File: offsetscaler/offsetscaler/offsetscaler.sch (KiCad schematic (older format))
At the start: 34 parts, among them J1 IN 1, J2 OUT 1, J3 INV OUT 1, J4 EURO_PWR_2x5, J5 IN 2, J6 OUT 2, J7 INV OUT 2, U1 TL074

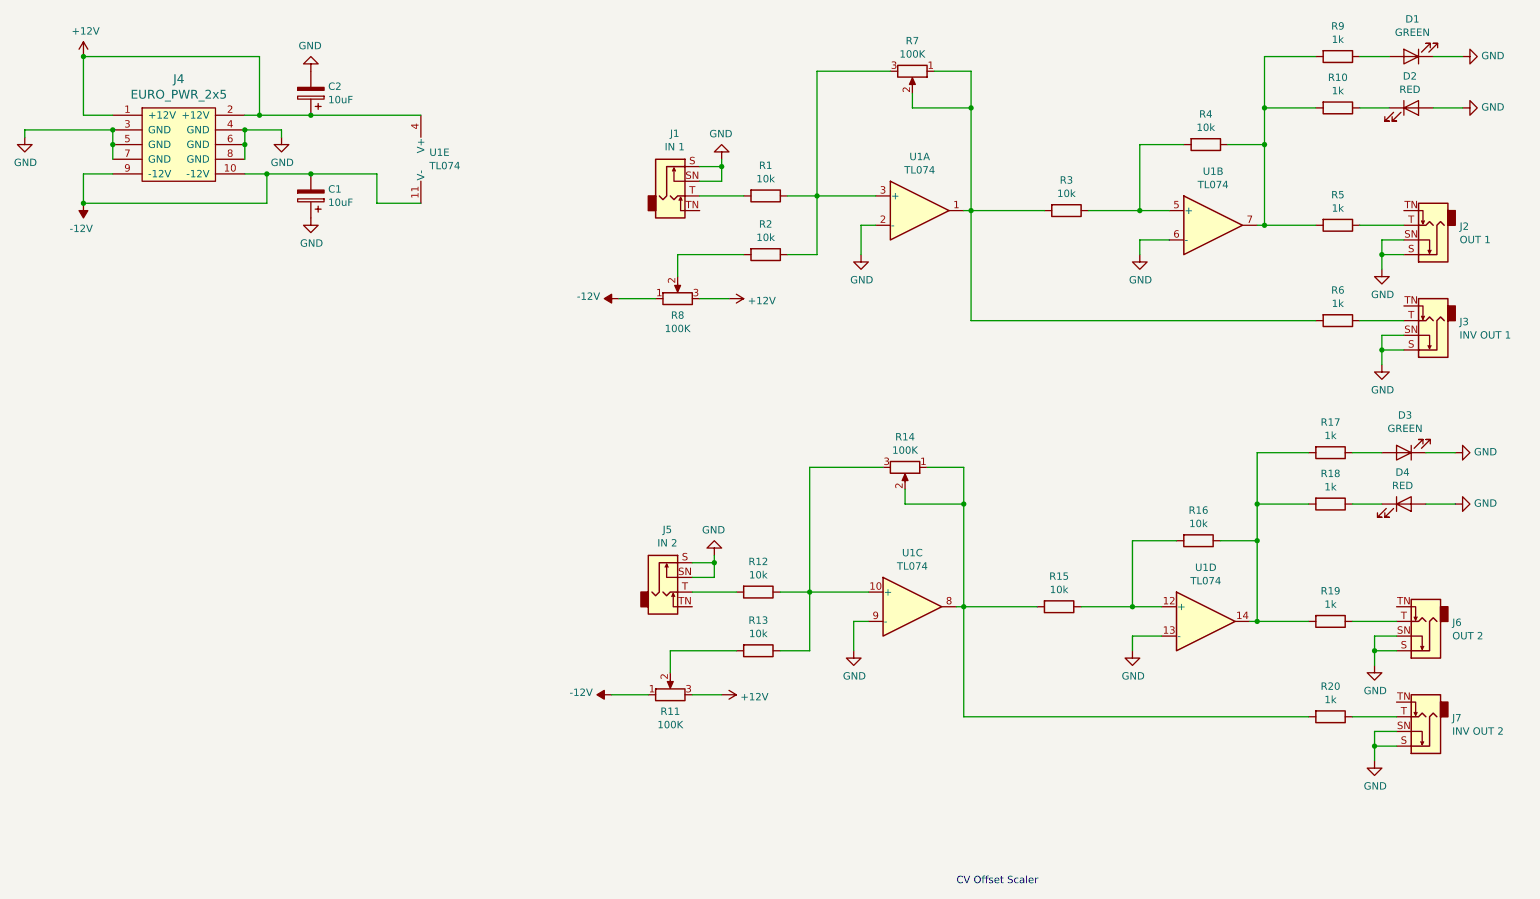
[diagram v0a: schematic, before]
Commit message: Fixed offsetscaler and added some megasequencer ideas and resources
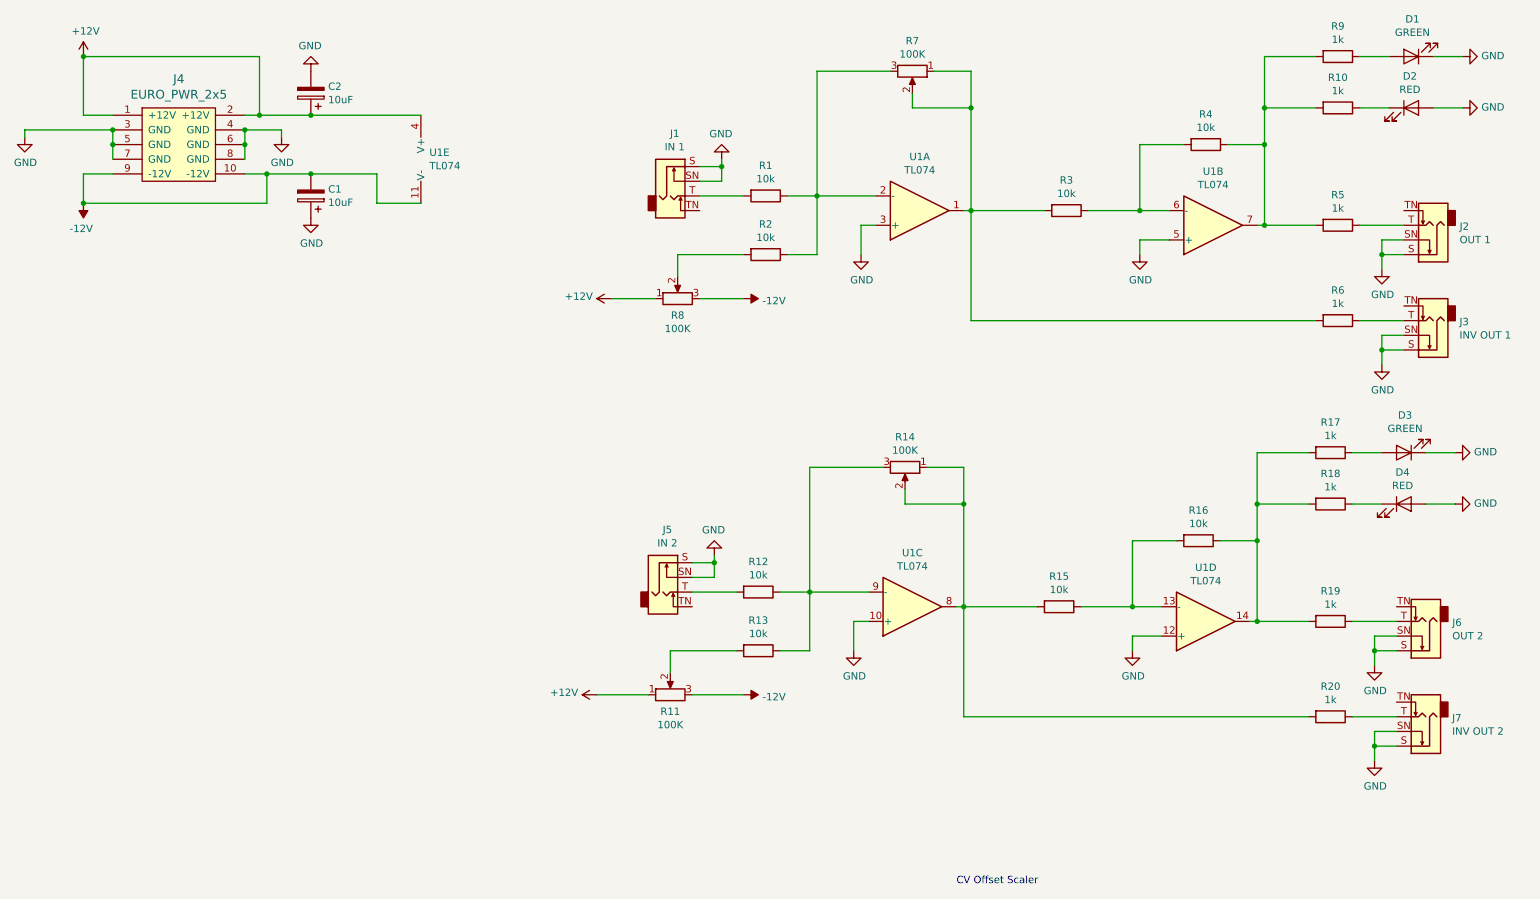
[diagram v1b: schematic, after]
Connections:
- net +12V: now also R11.1, R8.1; no longer R11.3, R8.3
- net -12V: now also R11.3, R8.3; no longer R11.1, R8.1
- net GND: now also U1.10 (+), U1.12 (+), U1.3 (+), U1.5 (+); no longer U1.13 (-), U1.2 (-), U1.6 (-), U1.9 (-)
- net at R1.1, R2.1, R7.3: now also U1.2 (-); no longer U1.3 (+)
- net at R3.1, R4.2: now also U1.6 (-); no longer U1.5 (+)
- net at R12.1, R13.1, R14.3: now also U1.9 (-); no longer U1.10 (+)
- net at R15.1, R16.2: now also U1.13 (-); no longer U1.12 (+)
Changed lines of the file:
@@
-$Comp
-L Amplifier_Operational:TL074 U1
-U 1 1 5D91D523
-P 6800 2100
-F 0 "U1" H 6800 2467 50  0000 C CNN
-F 1 "TL074" H 6800 2376 50  0000 C CNN
-F 2 "Package_DIP:DIP-14_W7.62mm_LongPads" H 6800 2100 50  0001 C CNN
-F 3 "http://www.ti.com/lit/ds/symlink/tl071.pdf" H 6800 2100 50  0001 C CNN
-	1    6800 2100
-	1    0    0    -1
-$EndComp
 $Comp
 L Amplifier_Operational:TL074 U1
 U 2 1 5D91D69A
 P 8800 2200
-F 0 "U1" H 8800 2567 50  0000 C CNN
-F 1 "TL074" H 8800 2476 50  0000 C CNN
+F 0 "U1" H 8800 1833 50  0000 C CNN
+F 1 "TL074" H 8800 1924 50  0000 C CNN
 F 2 "Package_DIP:DIP-14_W7.62mm_LongPads" H 8800 2200 50  0001 C CNN
 F 3 "http://www.ti.com/lit/ds/symlink/tl071.pdf" H 8800 2200 50  0001 C CNN
 	2    8800 2200
-	1    0    0    -1
+	1    0    0    1
 $EndComp
 $Comp
@@
 	1    0    0    -1
 $EndComp
-Wire Wire Line
-	8500 2300 8300 2300
-Wire Wire Line
-	8300 2300 8300 2400
-Wire Wire Line
-	6500 2200 6400 2200
-Wire Wire Line
-	6400 2200 6400 2400
 $Comp
 L Connector:AudioJack2_Switch J1
@@
 L power:+12V #PWR0108
 U 1 1 5D922076
-P 5500 2700
-F 0 "#PWR0108" H 5500 2550 50  0001 C CNN
-F 1 "+12V" V 5515 2828 50  0000 L CNN
-F 2 "" H 5500 2700 50  0001 C CNN
-F 3 "" H 5500 2700 50  0001 C CNN
-	1    5500 2700
-	0    1    1    0
+P 4700 2700
+F 0 "#PWR0108" H 4700 2550 50  0001 C CNN
+F 1 "+12V" V 4715 2828 50  0000 L CNN
+F 2 "" H 4700 2700 50  0001 C CNN
+F 3 "" H 4700 2700 50  0001 C CNN
+	1    4700 2700
+	0    -1   -1   0
 $EndComp
 $Comp
 L power:-12V #PWR0109
 U 1 1 5D9220B9
-P 4750 2700
-F 0 "#PWR0109" H 4750 2800 50  0001 C CNN
-F 1 "-12V" V 4765 2828 50  0000 L CNN
-F 2 "" H 4750 2700 50  0001 C CNN
-F 3 "" H 4750 2700 50  0001 C CNN
-	1    4750 2700
-	0    -1   -1   0
-$EndComp
-Wire Wire Line
-	4750 2700 5000 2700
-Wire Wire Line
-	5300 2700 5500 2700
+P 5600 2700
+F 0 "#PWR0109" H 5600 2800 50  0001 C CNN
+F 1 "-12V" V 5615 2828 50  0000 L CNN
+F 2 "" H 5600 2700 50  0001 C CNN
+F 3 "" H 5600 2700 50  0001 C CNN
+	1    5600 2700
+	0    1    1    0
+$EndComp
 $Comp
 L Device:R R2
@@
 	6100 2400 6100 2000
 Connection ~ 6100 2000
-Wire Wire Line
-	6100 2000 6500 2000
 $Comp
 L Device:R_POT R7
@@
 Wire Wire Line
 	8300 1650 8300 2100
-Connection ~ 8300 2100
-Wire Wire Line
-	8300 2100 8500 2100
 Wire Wire Line
 	8900 1650 9150 1650
@@
 	1    0    0    -1
 $EndComp
-Wire Wire Line
-	7100 2100 7150 2100
-Connection ~ 9150 2200
-Wire Wire Line
-	9150 2200 9100 2200
 Wire Wire Line
 	9150 2200 9500 2200
@@
 U 3 1 5D97E513
 P 6750 4800
-F 0 "U1" H 6750 5167 50  0000 C CNN
-F 1 "TL074" H 6750 5076 50  0000 C CNN
+F 0 "U1" H 6750 4433 50  0000 C CNN
+F 1 "TL074" H 6750 4524 50  0000 C CNN
 F 2 "Package_DIP:DIP-14_W7.62mm_LongPads" H 6750 4800 50  0001 C CNN
 F 3 "http://www.ti.com/lit/ds/symlink/tl071.pdf" H 6750 4800 50  0001 C CNN
 	3    6750 4800
-	1    0    0    -1
+	1    0    0    1
 $EndComp
 $Comp
@@
 U 4 1 5D97E519
 P 8750 4900
-F 0 "U1" H 8750 5267 50  0000 C CNN
-F 1 "TL074" H 8750 5176 50  0000 C CNN
+F 0 "U1" H 8750 4533 50  0000 C CNN
+F 1 "TL074" H 8750 4624 50  0000 C CNN
 F 2 "Package_DIP:DIP-14_W7.62mm_LongPads" H 8750 4900 50  0001 C CNN
 F 3 "http://www.ti.com/lit/ds/symlink/tl071.pdf" H 8750 4900 50  0001 C CNN
 	4    8750 4900
-	1    0    0    -1
+	1    0    0    1
 $EndComp
 $Comp
@@
 Wire Wire Line
 	8250 5000 8250 5100
-Wire Wire Line
-	6450 4900 6350 4900
-Wire Wire Line
-	6350 4900 6350 5100
 $Comp
 L Connector:AudioJack2_Switch J5
@@
 L power:+12V #PWR0117
 U 1 1 5D97E54E
-P 5450 5400
-F 0 "#PWR0117" H 5450 5250 50  0001 C CNN
-F 1 "+12V" V 5465 5528 50  0000 L CNN
-F 2 "" H 5450 5400 50  0001 C CNN
-F 3 "" H 5450 5400 50  0001 C CNN
-	1    5450 5400
-	0    1    1    0
+P 4600 5400
+F 0 "#PWR0117" H 4600 5250 50  0001 C CNN
+F 1 "+12V" V 4615 5528 50  0000 L CNN
+F 2 "" H 4600 5400 50  0001 C CNN
+F 3 "" H 4600 5400 50  0001 C CNN
+	1    4600 5400
+	0    -1   -1   0
 $EndComp
 $Comp
 L power:-12V #PWR0118
 U 1 1 5D97E554
-P 4700 5400
-F 0 "#PWR0118" H 4700 5500 50  0001 C CNN
-F 1 "-12V" V 4715 5528 50  0000 L CNN
-F 2 "" H 4700 5400 50  0001 C CNN
-F 3 "" H 4700 5400 50  0001 C CNN
-	1    4700 5400
-	0    -1   -1   0
-$EndComp
-Wire Wire Line
-	4700 5400 4950 5400
-Wire Wire Line
-	5250 5400 5450 5400
+P 5600 5400
+F 0 "#PWR0118" H 5600 5500 50  0001 C CNN
+F 1 "-12V" V 5615 5528 50  0000 L CNN
+F 2 "" H 5600 5400 50  0001 C CNN
+F 3 "" H 5600 5400 50  0001 C CNN
+	1    5600 5400
+	0    1    1    0
+$EndComp
 $Comp
 L Device:R R13
@@
 	6050 5100 6050 4700
 Connection ~ 6050 4700
-Wire Wire Line
-	6050 4700 6450 4700
 $Comp
 L Device:R_POT R14
@@
 	1    0    0    -1
 $EndComp
-Wire Wire Line
-	7050 4800 7100 4800
 Connection ~ 9100 4900
 Wire Wire Line
@@
 	2650 1450 3400 1450
 $Comp
-L power:GND #PWR?
+L power:GND #PWR0123
 U 1 1 5D9C92D6
 P 2650 1150
-F 0 "#PWR?" H 2650 900 50  0001 C CNN
+F 0 "#PWR0123" H 2650 900 50  0001 C CNN
 F 1 "GND" H 2655 977 50  0000 C CNN
 F 2 "" H 2650 1150 50  0001 C CNN
@@
 $EndComp
 $Comp
-L power:GND #PWR?
+L power:GND #PWR0124
 U 1 1 5D9C9379
 P 2650 2150
-F 0 "#PWR?" H 2650 1900 50  0001 C CNN
+F 0 "#PWR0124" H 2650 1900 50  0001 C CNN
 F 1 "GND" H 2655 1977 50  0000 C CNN
 F 2 "" H 2650 2150 50  0001 C CNN
@@
 	1    0    0    -1
 $EndComp
+Wire Wire Line
+	4700 2700 5000 2700
+Wire Wire Line
+	5300 2700 5600 2700
+Wire Wire Line
+	4600 5400 4950 5400
+Wire Wire Line
+	5250 5400 5600 5400
+$Comp
+L Amplifier_Operational:TL074 U1
+U 1 1 5D91D523
+P 6800 2100
+F 0 "U1" H 6800 1733 50  0000 C CNN
+F 1 "TL074" H 6800 1824 50  0000 C CNN
+F 2 "Package_DIP:DIP-14_W7.62mm_LongPads" H 6800 2100 50  0001 C CNN
+F 3 "http://www.ti.com/lit/ds/symlink/tl071.pdf" H 6800 2100 50  0001 C CNN
+	1    6800 2100
+	1    0    0    1
+$EndComp
+Wire Wire Line
+	6100 2000 6500 2000
+Wire Wire Line
+	6400 2200 6400 2400
+Wire Wire Line
+	6400 2200 6500 2200
+Wire Wire Line
+	7100 2100 7150 2100
+Wire Wire Line
+	8300 2100 8500 2100
+Connection ~ 8300 2100
+Wire Wire Line
+	8500 2300 8300 2300
+Wire Wire Line
+	8300 2300 8300 2400
+Wire Wire Line
+	9100 2200 9150 2200
+Connection ~ 9150 2200
+Wire Wire Line
+	6050 4700 6450 4700
+Wire Wire Line
+	6450 4900 6350 4900
+Wire Wire Line
+	6350 4900 6350 5100
+Wire Wire Line
+	7050 4800 7100 4800
 $EndSCHEMATC
